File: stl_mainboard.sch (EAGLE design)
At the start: 45 parts, among them IC1 LM555D, IC2 4017D, IC4 ULN2001AD, Q1 AUIRFR5305, Q2 AUIRFR5305, Q3 AUIRFR5305, Q4 AUIRFR5305, Q5 AUIRFR5305, Q6 AUIRFR5305, Q7 AUIRFR5305

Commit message: mainboard in progress
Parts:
- removed IC4: ULN2001AD, uln-udn:ULN2001AD
- added C4: 0.1uF, rcl:C-USC0805
- added D8: BAS40, diode:BAS40
- added IC3: ULN2001AD, uln-udn:ULN2001AD
- C3: device rcl:C-USC1206 -> rcl:C-USC0805
- D1: value BAS40 -> 48CTQ060S; device diode:BAS40 -> diode:BY229B
- D2: value BAS40 -> SMBJ15; device diode:BAS40 -> diode:SUPPRESSOR-SMBJ
- D6: value SMBJ15 -> BAS40; device diode:SUPPRESSOR-SMBJ -> diode:BAS40
- D7: value 48CTQ060S -> BAS40; device diode:BY229B -> diode:BAS40
- R1, R11, R12, R13, R15, R17, R4, R5, R6, R7, R8, R9: device rcl:R-US_M1206 -> rcl:R-US_M0805
- R10, R18: value 1K -> 0; device rcl:R-US_M1206 -> rcl:R-US_M0805
- R14, R16: value 0 -> 1K
- R2: value 4K2 -> 1K; device rcl:R-US_M1206 -> rcl:R-US_M0805
- R3: value 1K -> 4K2; device rcl:R-US_M1206 -> rcl:R-US_M0805
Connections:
- removed net GND: D6.A, IC2A.RES, IC4.GND, R3.2, X1-2.KL
- removed net N$11: D7.2, X1-1.KL
- net +12V: now also D1.2, X1-1.KL, X2-8.KL; no longer D6.C, D7.1, D7.K, Q1.S, Q2.S, Q3.S, Q4.S, Q5.S, Q6.S, Q7.S, R10.1, R18.1, R19.1, R20.1, R21.1, R22.1, R23.1
- net BULB2: now also X2-7.KL
- net BULB2_CTRL: now also IC3.O1, R14.2; no longer IC4.O1, R10.2
- net BULB3: now also Q3.D, X2-6.KL; no longer Q2.D
- net BULB3_CTRL: now also IC3.O2, Q3.G, R19.2; no longer IC4.O2, Q2.G, R18.2
- net BULB4: now also Q6.D, X2-5.KL; no longer Q3.D
- net BULB4_CTRL: now also IC3.O3, Q6.G, R22.2; no longer IC4.O3, Q3.G, R19.2
- net BULB5: now also Q7.D, X2-4.KL; no longer Q4.D
- net BULB5_CTRL: now also IC3.O4, Q7.G, R23.2; no longer IC4.O4, Q4.G, R20.2
- net BULB6: now also Q2.D, X2-3.KL; no longer Q5.D
- net BULB6_CTRL: now also IC3.O5, Q2.G, R16.2; no longer IC4.O5, Q5.G, R21.2
- net BULB7: now also Q4.D, X2-2.KL; no longer Q6.D
- net BULB7_CTRL: now also IC3.O6, Q4.G, R20.2; no longer IC4.O6, Q6.G, R22.2
- net BULB8: now also Q5.D, X2-1.KL; no longer Q7.D
- net BULB8_CTRL: now also IC3.O7, Q5.G, R21.2; no longer IC4.O7, Q7.G, R23.2
- net CNTR_STOP: now also R1.1, R11.2, R12.2, R13.2, R15.2, R17.2, R18.2; no longer R3.1, R4.2, R5.2, R6.2, R7.2, R8.2, R9.2
- net N$10: now also R6.1; no longer R17.1
- net N$2: now also R3.1; no longer R1.1
- net N$3: now also R3.2; no longer R2.2
- net N$4: now also R4.1; no longer R11.1
- net N$5: now also R7.1; no longer R12.1
- net N$6: now also R9.1; no longer R13.1
- net N$7: now also R5.1; no longer R14.1
- net N$8: now also R8.1; no longer R15.1
- net N$9: now also R10.1; no longer R16.1
- net Q0: now also D3.C, IC3.I5, R4.2; no longer IC4.I1, R11.2
- net Q1: now also D3.A, D4.C, IC3.I6, R11.1, R7.2; no longer D1.C, IC4.I2, R12.2, R5.1
- net Q2: now also D4.A, D5.C, IC3.I4, R12.1, R9.2; no longer D1.A, D2.C, IC4.I3, R13.2, R6.1
- net Q3: now also D5.A, D6.C, IC3.I1, R13.1, R5.2; no longer D2.A, D3.C, IC4.I4, R14.2, R7.1
- net Q4: now also D6.A, D7.C, IC3.I2, R15.1, R8.2; no longer D3.A, D4.C, IC4.I5, R15.2, R8.1
- net Q5: now also D7.A, D8.C, IC3.I7, R10.2, R17.1; no longer D4.A, D5.C, IC4.I6, R16.2, R4.1
- net Q6: now also D8.A, IC3.I3, R18.1, R6.2; no longer D5.A, IC4.I7, R17.2, R9.1
- net VDD: now also C4.1, D1.1, D1.K, D2.C, Q1.S, Q2.S, Q3.S, Q4.S, Q5.S, Q6.S, Q7.S, R14.1, R16.1, R19.1, R2.2, R20.1, R21.1, R22.1, R23.1; no longer R1.2
- net VSS: now also C4.2, D2.A, IC2A.RES, IC3.GND, R1.2, X1-2.KL
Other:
- moved on the sheet: D3, D4, D5, Q2, Q3, Q4, Q5, Q6, Q7, R1, R10, R11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

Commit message: board and schematics done
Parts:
- removed D3, D4, D5, D6, D7, D8: BAS40, diode:BAS40
- removed X2: (no value), con-wago-508:W237-08P
- added D10, D11, D9: BAS40-04, diode:BAS40-04
- added X3: (no value), con-wago-508:W237-09P
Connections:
- removed net +12V: D1.2, X1-1.KL, X2-8.KL
- new net B+: D1.2, X1-1.KL, X3-1.KL
- net BULB2: now also X3-2.KL; no longer X2-7.KL
- net BULB3: now also X3-3.KL; no longer X2-6.KL
- net BULB4: now also X3-4.KL; no longer X2-5.KL
- net BULB5: now also X3-5.KL; no longer X2-4.KL
- net BULB6: now also X3-6.KL; no longer X2-3.KL
- net BULB7: now also X3-7.KL; no longer X2-2.KL
- net BULB8: now also X3-8.KL; no longer X2-1.KL
- net Q0: now also D9.C2; no longer D3.C
- net Q1: now also D9.C1A2; no longer D3.A, D4.C
- net Q2: now also D10.C2, D9.A1; no longer D4.A, D5.C
- net Q3: now also D10.C1A2; no longer D5.A, D6.C
- net Q4: now also D10.A1, D11.C2; no longer D6.A, D7.C
- net Q5: now also D11.C1A2; no longer D7.A, D8.C
- net Q6: now also D11.A1; no longer D8.A
- net VSS: now also X3-9.KL
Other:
- moved on the sheet: IC3

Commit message: No more 555 and 4017. STM8 instead.
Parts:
- removed D10, D11, D9: BAS40-04, diode:BAS40-04
- removed R19, R20, R21, R22, R23: 1K, rcl:R-US_M1206
- removed X3: (no value), con-wago-508:W237-09P
- added LED1: (no value), led:LEDSML1206
- added SV1: (no value), con-lstb:MA04-1
- added X2: (no value), con-wago-508:W237-09P
- C1: value 47 -> 1uF; device rcl:CPOL-USE5-8.5 -> rcl:C-EUC1206
- C2: value 0.01 -> 100nf; device rcl:C-USC1206 -> rcl:C-EUC1206
- C3: value 0.1uF -> 0.33; device rcl:C-USC0805 -> rcl:CPOL-USE5-8.5
- C4: value 0.1uF -> 0.1
- D1: value 48CTQ060S -> 48CTQ060; device diode:BY229B -> 48ctq060:48CTQ060
- IC1: value LM555D -> STM8S003F3; device linear:LM555D -> stm8:STM8S003F3
- IC2: value 4017D -> 78L05F; device 40xx:4017D -> linear:78L05F
- R10, R11, R12, R13, R15, R4: value 0 -> 1K
- R14, R16: device rcl:R-US_M1206 -> rcl:R-US_M0805
- R3: value 4K2 -> 1K
- R5: value 0 -> 5k6
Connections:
- removed net BULB2: Q1.D, X3-2.KL
- removed net BULB2_CTRL: IC3.O1, Q1.G, R14.2
- removed net BULB3: Q3.D, X3-3.KL
- removed net BULB3_CTRL: IC3.O2, Q3.G, R19.2
- removed net BULB4: Q6.D, X3-4.KL
- removed net BULB4_CTRL: IC3.O3, Q6.G, R22.2
- removed net BULB5: Q7.D, X3-5.KL
- removed net BULB5_CTRL: IC3.O4, Q7.G, R23.2
- removed net BULB6: Q2.D, X3-6.KL
- removed net BULB6_CTRL: IC3.O5, Q2.G, R16.2
- removed net BULB7: Q4.D, X3-7.KL
- removed net BULB7_CTRL: IC3.O6, Q4.G, R20.2
- removed net BULB8: Q5.D, X3-8.KL
- removed net BULB8_CTRL: IC3.O7, Q5.G, R21.2
- removed net CNTR_STOP: IC2A.ENA, R1.1, R11.2, R12.2, R13.2, R15.2, R17.2, R18.2
- removed net N$4: IC2A.Q0, R4.1
- removed net Q0: D9.C2, IC3.I5, R4.2
- removed net Q1: D9.C1A2, IC3.I6, R11.1, R7.2
- removed net Q2: D10.C2, D9.A1, IC3.I4, R12.1, R9.2
- removed net Q3: D10.C1A2, IC3.I1, R13.1, R5.2
- removed net Q4: D10.A1, D11.C2, IC3.I2, R15.1, R8.2
- removed net Q5: D11.C1A2, IC3.I7, R10.2, R17.1
- removed net Q6: D11.A1, IC3.I3, R18.1, R6.2
- removed net TMR_OUT: IC1.Q, IC2A.CLK
- removed net VSS: C1.-, C2.2, C3.2, C4.2, D2.A, IC1.GND, IC2A.RES, IC3.GND, R1.2, X1-2.KL, X3-9.KL
- new net +5V: C2.1, C4.1, IC1.VDD, IC2.VO, R1.1, R17.2, R18.2, R9.2, SV1.4
- new net BULB01: Q2.D, X2-7.KL
- new net BULB01_CTRL: IC3.O1, Q2.G, R11.2
- new net BULB02: Q4.D, X2-6.KL
- new net BULB02_CTRL: IC3.O2, Q4.G, R13.2
- new net BULB03: Q5.D, X2-5.KL
- new net BULB03_CTRL: IC3.O3, Q5.G, R14.2
- new net BULB04: Q1.D, X2-4.KL
- new net BULB04_CTRL: IC3.O4, Q1.G, R10.2
- new net BULB05: Q3.D, X2-3.KL
- new net BULB05_CTRL: IC3.O5, Q3.G, R12.2
- new net BULB06: Q6.D, X2-2.KL
- new net BULB06_CTRL: IC3.O6, Q6.G, R15.2
- new net BULB07: Q7.D, X2-1.KL
- new net BULB07_CTRL: IC3.O7, Q7.G, R16.2
- new net GND: C1.2, C2.2, C3.-, C4.2, D2.A, IC1.GND, IC2.GND, IC2.GND@1, IC3.GND, R5.2, R6.1, R7.1, R8.1, SV1.2, X1-2.KL, X2-9.KL
- new net NRST: IC1.!RST, R1.2, SV1.1
- new net Q01: IC1.PC7/SPI_MISO/[TIM1_CH2], IC3.I1
- new net Q02: IC1.PC6/SPI_MOSI/[TIM1_CH1], IC3.I2
- new net Q03: IC1.PC5/SPI_SCK/[TIM2_CH1], IC3.I3
- new net Q04: IC1.PC4/TIM1_CH4/CLK_CCO/AIN2/[!TIM1_CH2!], IC3.I4
- new net Q05: IC1.PC3/TIM1_CH3/[TLI]/[!TIM1_CH1!], IC3.I5
- new net Q06: IC1.PB4/I2C_SCL/[ADC_ETR], IC3.I6
- new net Q07: IC1.PB5/I2C_SDA/[TIM1_BKIN], IC3.I7
- new net SWIM: IC1.PD1/SWIM, SV1.3
- net B+: now also D1.P$2, D1.P$3, X2-8.KL; no longer D1.2, X3-1.KL
- net N$1: now also IC1.PA3/TIM2_CH3/[SPI_NSS], LED1.A; no longer C2.1, IC1.CV
- net N$10: now also R18.1, R4.2, R6.2; no longer IC2A.Q6, R6.1
- net N$2: now also LED1.C, R5.1; no longer IC1.DIS, R2.1, R3.1
- net N$3: now also C1.1, IC1.VCAP; no longer C1.+, IC1.THR, IC1.TR, R3.2
- net N$5: now also IC1.PD4/UART1_CK/TIM2_CH1/BEEP, R3.1; no longer IC2A.Q1, R7.1
- net N$6: now also IC1.PD5/UART1_TX/AIN5, R2.1; no longer IC2A.Q2, R9.1
- net N$7: now also IC1.PD6/UART1_RX/AIN6, R4.1; no longer IC2A.Q3, R5.1
- net N$8: now also R3.2, R8.2, R9.1; no longer IC2A.Q4, R8.1
- net N$9: now also R17.1, R2.2, R7.2; no longer IC2A.Q5, R10.1
- net VDD: now also C3.+, D1.P$1, IC2.VI, R10.1, R11.1, R12.1, R13.1, R15.1; no longer C3.1, C4.1, D1.1, D1.K, IC1.R, IC1.V+, R19.1, R2.2, R20.1, R21.1, R22.1, R23.1
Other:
- note removed: "This resistors select upper limit for counter"
- note removed: "Tiimer period must be 300ms approx"
- moved on the sheet: C2, C4, D2, IC3, R1, R10, R11, R12, R13, R14, R15, R16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

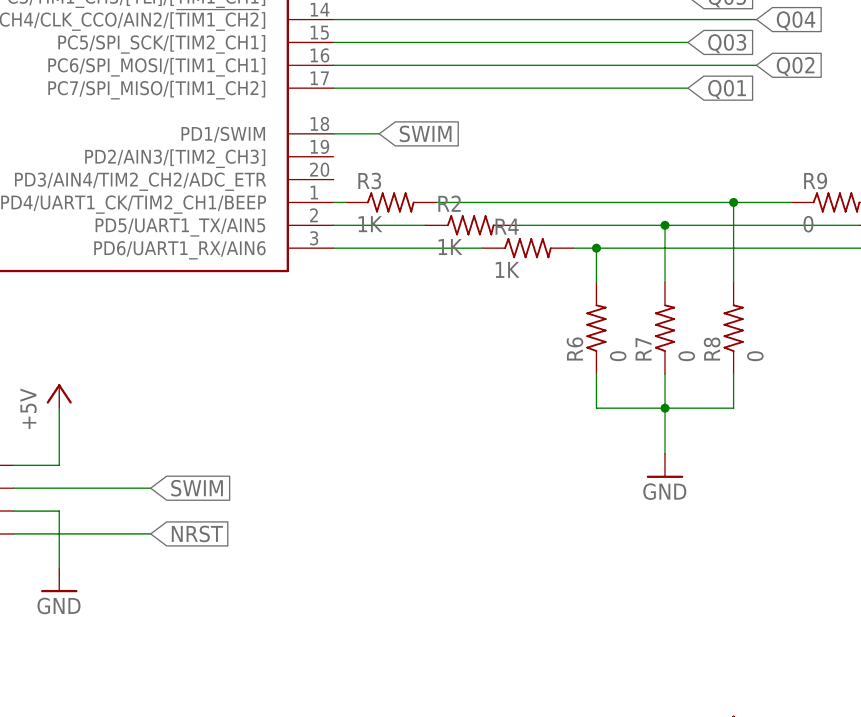
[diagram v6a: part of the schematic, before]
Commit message: Added 'LEARN' jumper
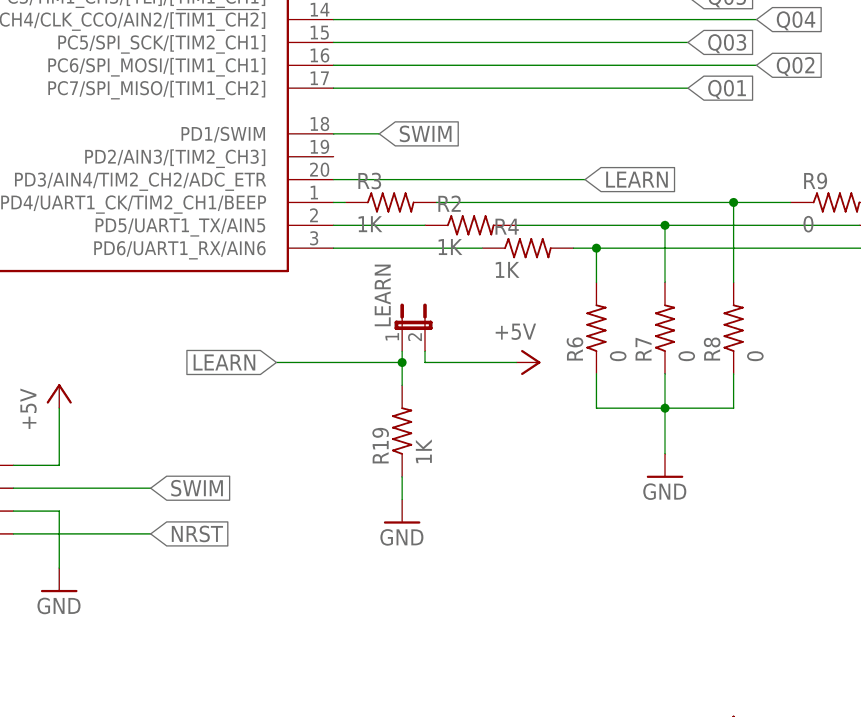
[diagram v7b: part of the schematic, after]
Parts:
- added LEARN: (no value), jumper:JP1E
- added R19: 1K, rcl:R-US_M0805
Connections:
- new net LEARN: IC1.PD3/AIN4/TIM2_CH2/ADC_ETR, LEARN.1, R19.2
- net +5V: now also LEARN.2
- net GND: now also R19.1
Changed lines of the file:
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@@
 <grid distance="0.05" unitdist="inch" unit="inch" style="lines" multiple="1" display="no" altdistance="0.0025" altunitdist="inch" altunit="inch"/>
 <layers>
-<layer number="1" name="Top" color="4" fill="1" visible="yes" active="no"/>
-<layer number="16" name="Bottom" color="1" fill="1" visible="yes" active="no"/>
-<layer number="17" name="Pads" color="2" fill="1" visible="yes" active="no"/>
-<layer number="18" name="Vias" color="2" fill="1" visible="yes" active="no"/>
-<layer number="19" name="Unrouted" color="6" fill="1" visible="yes" active="no"/>
-<layer number="20" name="Dimension" color="15" fill="1" visible="yes" active="no"/>
-<layer number="21" name="tPlace" color="7" fill="1" visible="yes" active="no"/>
-<layer number="22" name="bPlace" color="7" fill="1" visible="yes" active="no"/>
-<layer number="23" name="tOrigins" color="15" fill="1" visible="yes" active="no"/>
-<layer number="24" name="bOrigins" color="15" fill="1" visible="yes" active="no"/>
-<layer number="25" name="tNames" color="7" fill="1" visible="yes" active="no"/>
-<layer number="26" name="bNames" color="7" fill="1" visible="yes" active="no"/>
-<layer number="27" name="tValues" color="7" fill="1" visible="yes" active="no"/>
-<layer number="28" name="bValues" color="7" fill="1" visible="yes" active="no"/>
+<layer number="1" name="Top" color="4" fill="1" visible="no" active="no"/>
+<layer number="16" name="Bottom" color="1" fill="1" visible="no" active="no"/>
+<layer number="17" name="Pads" color="2" fill="1" visible="no" active="no"/>
+<layer number="18" name="Vias" color="2" fill="1" visible="no" active="no"/>
+<layer number="19" name="Unrouted" color="6" fill="1" visible="no" active="no"/>
+<layer number="20" name="Dimension" color="15" fill="1" visible="no" active="no"/>
+<layer number="21" name="tPlace" color="7" fill="1" visible="no" active="no"/>
+<layer number="22" name="bPlace" color="7" fill="1" visible="no" active="no"/>
+<layer number="23" name="tOrigins" color="15" fill="1" visible="no" active="no"/>
+<layer number="24" name="bOrigins" color="15" fill="1" visible="no" active="no"/>
+<layer number="25" name="tNames" color="7" fill="1" visible="no" active="no"/>
+<layer number="26" name="bNames" color="7" fill="1" visible="no" active="no"/>
+<layer number="27" name="tValues" color="7" fill="1" visible="no" active="no"/>
+<layer number="28" name="bValues" color="7" fill="1" visible="no" active="no"/>
 <layer number="29" name="tStop" color="7" fill="3" visible="no" active="no"/>
 <layer number="30" name="bStop" color="7" fill="6" visible="no" active="no"/>
@@
 <layer number="35" name="tGlue" color="7" fill="4" visible="no" active="no"/>
 <layer number="36" name="bGlue" color="7" fill="5" visible="no" active="no"/>
-<layer number="37" name="tTest" color="7" fill="1" visible="yes" active="no"/>
-<layer number="38" name="bTest" color="7" fill="1" visible="yes" active="no"/>
+<layer number="37" name="tTest" color="7" fill="1" visible="no" active="no"/>
+<layer number="38" name="bTest" color="7" fill="1" visible="no" active="no"/>
 <layer number="39" name="tKeepout" color="4" fill="11" visible="no" active="no"/>
 <layer number="40" name="bKeepout" color="1" fill="11" visible="no" active="no"/>
@@
 <layer number="44" name="Drills" color="7" fill="1" visible="no" active="no"/>
 <layer number="45" name="Holes" color="7" fill="1" visible="no" active="no"/>
-<layer number="46" name="Milling" color="3" fill="1" visible="yes" active="no"/>
-<layer number="47" name="Measures" color="7" fill="1" visible="yes" active="no"/>
-<layer number="48" name="Document" color="7" fill="1" visible="yes" active="no"/>
-<layer number="49" name="Reference" color="7" fill="1" visible="yes" active="no"/>
-<layer number="51" name="tDocu" color="7" fill="1" visible="yes" active="no"/>
-<layer number="52" name="bDocu" color="7" fill="1" visible="yes" active="no"/>
+<layer number="46" name="Milling" color="3" fill="1" visible="no" active="no"/>
+<layer number="47" name="Measures" color="7" fill="1" visible="no" active="no"/>
+<layer number="48" name="Document" color="7" fill="1" visible="no" active="no"/>
+<layer number="49" name="Reference" color="7" fill="1" visible="no" active="no"/>
+<layer number="51" name="tDocu" color="7" fill="1" visible="no" active="no"/>
+<layer number="52" name="bDocu" color="7" fill="1" visible="no" active="no"/>
 <layer number="90" name="Modules" color="5" fill="1" visible="yes" active="yes"/>
 <layer number="91" name="Nets" color="2" fill="1" visible="yes" active="yes"/>
@@
 <part name="R18" library="rcl" deviceset="R-US_" device="M0805" value="0"/>
 <part name="P+7" library="supply1" deviceset="+5V" device=""/>
+<part name="LEARN" library="jumper" deviceset="JP1E" device=""/>
+<part name="R19" library="rcl" deviceset="R-US_" device="M0805" value="1K"/>
+<part name="P+8" library="supply1" deviceset="+5V" device=""/>
+<part name="GND9" library="supply1" deviceset="GND" device=""/>
 </parts>
 <sheets>
@@
 <instance part="R18" gate="G$1" x="44.45" y="88.9"/>
 <instance part="P+7" gate="1" x="60.96" y="96.52"/>
+<instance part="LEARN" gate="A" x="-17.78" y="80.01"/>
+<instance part="R19" gate="G$1" x="-17.78" y="68.58" rot="R90"/>
+<instance part="P+8" gate="1" x="-2.54" y="76.2" rot="R270"/>
+<instance part="GND9" gate="1" x="-17.78" y="58.42"/>
 </instances>
 <busses>
@@
 <wire x1="43.18" y1="91.44" x2="52.07" y2="91.44" width="0.1524" layer="91"/>
 </segment>
+<segment>
+<pinref part="LEARN" gate="A" pin="2"/>
+<wire x1="-15.24" y1="77.47" x2="-15.24" y2="76.2" width="0.1524" layer="91"/>
+<wire x1="-15.24" y1="76.2" x2="-5.08" y2="76.2" width="0.1524" layer="91"/>
+<pinref part="P+8" gate="1" pin="+5V"/>
+</segment>
 </net>
 <net name="NRST" class="0">
@@
 <wire x1="226.06" y1="29.21" x2="226.06" y2="26.67" width="0.1524" layer="91"/>
 </segment>
+<segment>
+<pinref part="R19" gate="G$1" pin="1"/>
+<pinref part="GND9" gate="1" pin="GND"/>
+<wire x1="-17.78" y1="63.5" x2="-17.78" y2="60.96" width="0.1524" layer="91"/>
+</segment>
 </net>
 <net name="N$3" class="0">
@@
 </segment>
 </net>
+<net name="LEARN" class="0">
+<segment>
+<pinref part="IC1" gate="G$1" pin="PD3/AIN4/TIM2_CH2/ADC_ETR"/>
+<wire x1="-25.4" y1="96.52" x2="2.54" y2="96.52" width="0.1524" layer="91"/>
+<label x="2.54" y="96.52" size="1.778" layer="95" xref="yes"/>
+</segment>
+<segment>
+<pinref part="LEARN" gate="A" pin="1"/>
+<pinref part="R19" gate="G$1" pin="2"/>
+<wire x1="-17.78" y1="77.47" x2="-17.78" y2="76.2" width="0.1524" layer="91"/>
+<wire x1="-17.78" y1="76.2" x2="-17.78" y2="73.66" width="0.1524" layer="91"/>
+<wire x1="-17.78" y1="76.2" x2="-31.75" y2="76.2" width="0.1524" layer="91"/>
+<junction x="-17.78" y="76.2"/>
+<label x="-31.75" y="76.2" size="1.778" layer="95" rot="R180" xref="yes"/>
+</segment>
+</net>
